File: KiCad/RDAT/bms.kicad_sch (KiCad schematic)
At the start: 29 parts, among them Q1 NMOS, Q2 NMOS, U3 BQ7791500PWT, U4 BQ34Z100PWR-R2

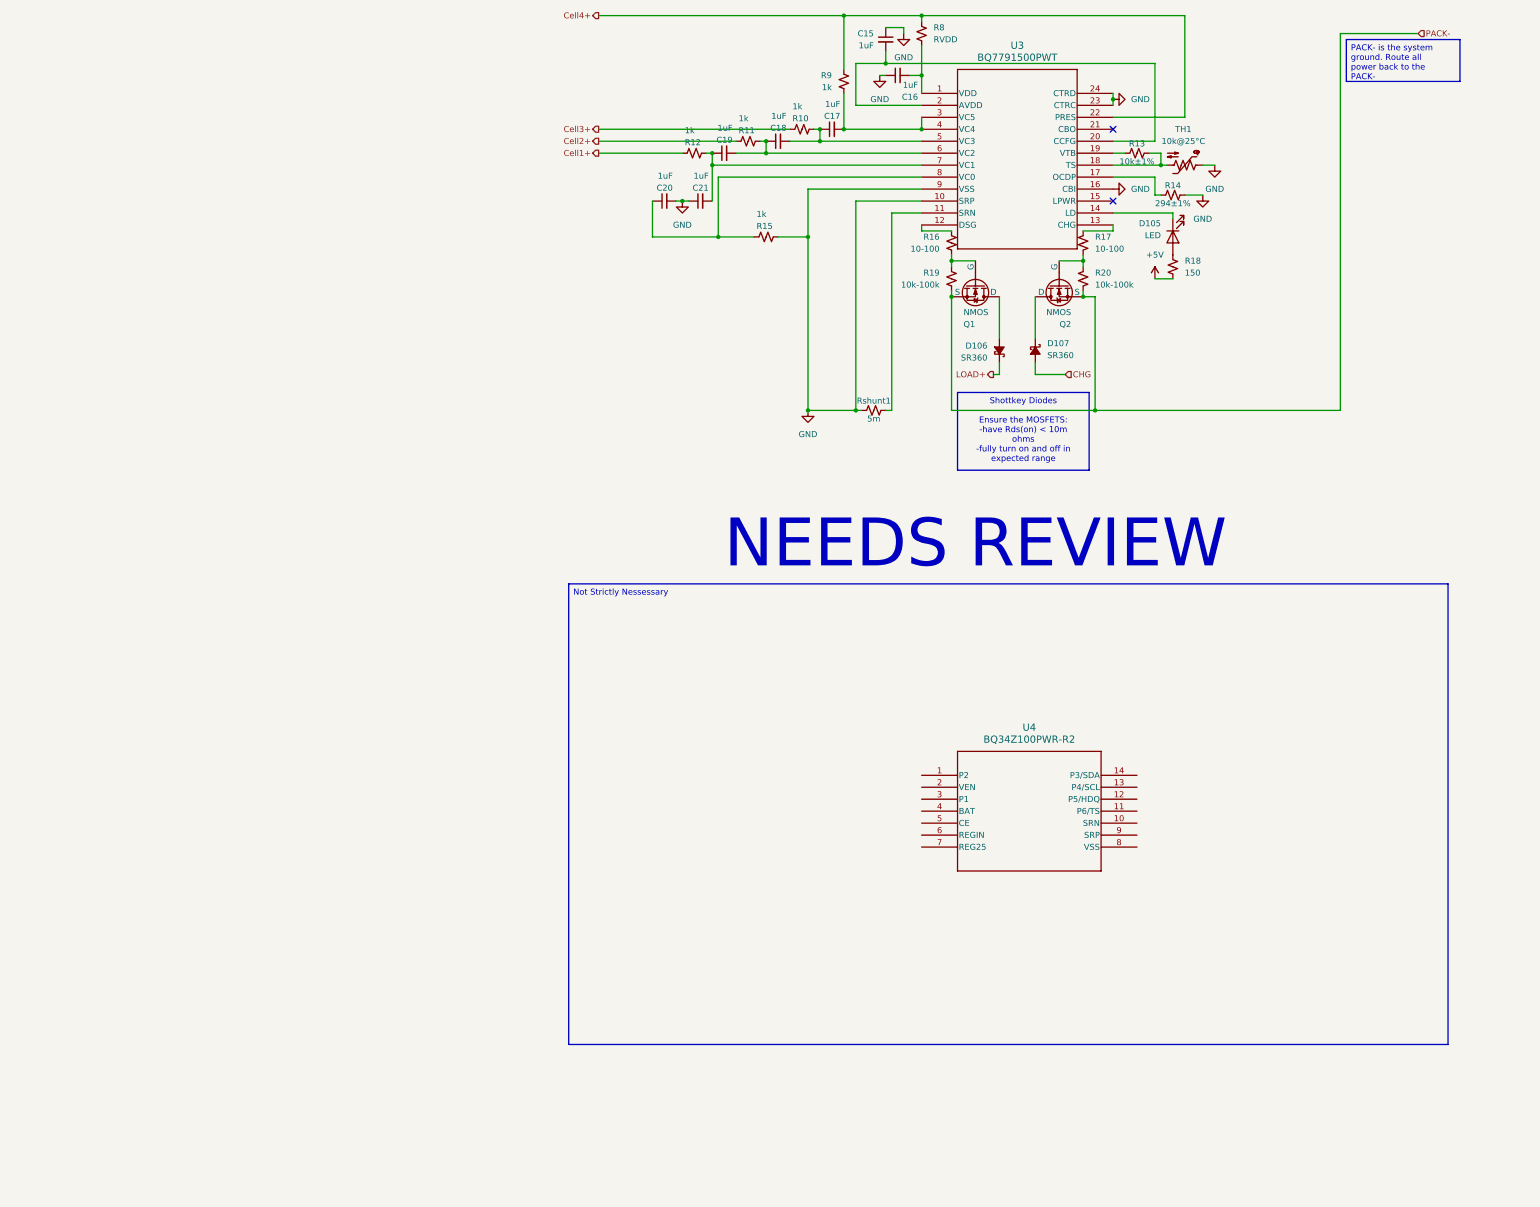
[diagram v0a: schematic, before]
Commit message: Started process of BMS review
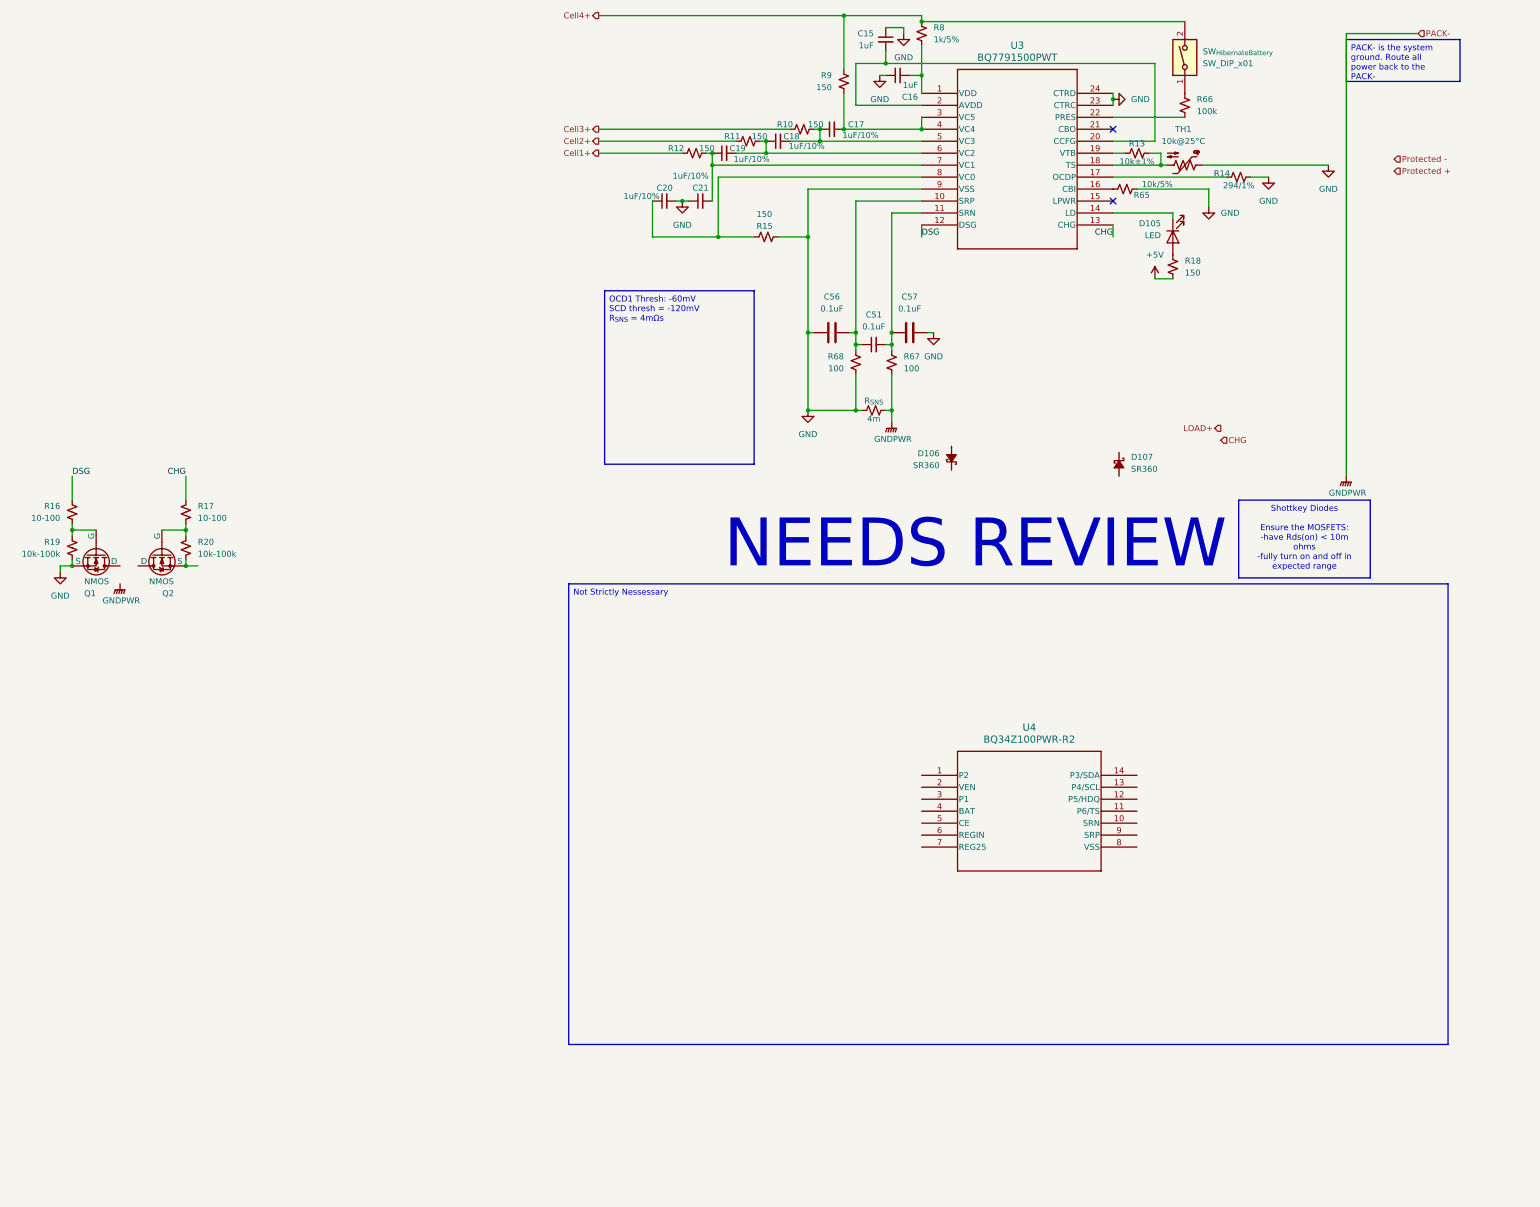
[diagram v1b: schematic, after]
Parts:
- added C51: 0.1uF, symbol Device:C_Small
- added C56, C57: 0.1uF, symbol Device:C
- added R65: 10k/5%, symbol Device:R_Small_US
- added R66: 100k, symbol Device:R_Small_US
- added R67, R68: 100, symbol Device:R_Small_US
- added SW_{HibernateBattery}: SW_DIP_x01, symbol Switch:SW_DIP_x01
- C17, C18, C19, C20, C21: value 1uF -> 1uF/10%
- R10, R11, R12, R15, R9: value 1k -> 150
- R14: value 294±1% -> 294/1%
- R8: value RVDD -> 1k/5%
- R_{SNS}: renamed from Rshunt1; value 5m -> 4m
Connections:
- net CHG: now also R17.1, U3.13 (CHG); no longer D107.2 (A)
- net Cell4+: now also SW_{HibernateBattery}.2; no longer U3.22 (PRES)
- net GND: now also Q1.3 (S), R19.2, C56.1, C57.2, R65.2, R68.2; no longer U3.10 (SRP), U3.16 (CBI)
- net LOAD+: no longer D106.1 (K)
- net at Q2.1 (D): no longer D107.1 (K)
- net at U3.11 (SRN): now also C51.2, C57.1, R67.1; no longer R_{SNS}.2
- net DSG: now reaches R16.1, U3.12 (DSG)
- net at Q1.1 (D): no longer D106.2 (A)
- net PACK-: no longer names the net of Q2.3 (S), R20.2
- net PACK-: no longer Q1.3 (S), R19.2
- new net: C51.1, C56.2, R68.1, U3.10 (SRP)
- new net: R66.1, SW_{HibernateBattery}.1
- new net: R66.2, U3.22 (PRES)
- new net: R65.1, U3.16 (CBI)
- new net GNDPWR: R67.2, R_{SNS}.2
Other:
- moved on the sheet: D106, D107, Q1, Q2, R14, R16, R17, R19, R20

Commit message: 2x checked all schematics
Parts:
- removed C18, C19, C20, C21: 1uF/10%, symbol Device:C_Small
- removed C51: 0.1uF, symbol Device:C_Small
- removed C56, C57: 0.1uF, symbol Device:C
- removed D105: LED, symbol Device:LED
- removed D106, D107: SR360, symbol Device:D_Schottky_Small_Filled
- removed R11, R12, R15, R18: 150, symbol Device:R_Small_US
- removed R14: 294/1%, symbol Device:R_Small_US
- removed R65: 10k/5%, symbol Device:R_Small_US
- removed R67, R68: 100, symbol Device:R_Small_US
- removed R_{SNS}: 4m, symbol Device:R_Small_US
- added C58, C59, C62, C63: 1uF/10%, symbol Device:C_Small
- added C64, C67: 0.1uF, symbol Device:C
- added C65: 0.1uF, symbol Device:C_Small
- added R101, R103, R94: 150, symbol Device:R_Small_US
- added R102, R104: 100, symbol Device:R_Small_US
- added R16: R_Small_US, symbol Device:R_Small_US
- added R17: 470, symbol Device:R_Small_US
- added R85: 1k/5%, symbol Device:R_Small_US
- added R_{SNS}1: 4m, symbol Device:R_Small_US
- R8: value 1k/5% -> 450k
- R_{CHG}1: renamed from R17; value 10-100 -> 220/5%
- R_{DSG}1: renamed from R16; value 10-100 -> 470/5%
- R_{GS}1: renamed from R19; value 10k-100k -> 4.7M
- R_{GS}2: renamed from R20; value 10k-100k -> 4.7M
- U4: now not fitted
- renumbered SW_{HibernateBattery} to SW_{HibernateBattery}1, TH1 to TH_103AT_1
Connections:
- net Cell1+: now also R101.2
- net Cell2+: now also R94.2
- net Cell3+: now also R10.2; no longer R10.1
- net Cell4+: now also R85.1; no longer R8.1
- net SRP: now reaches U3.10 (SRP)
- net SRP: now also C65.2, C67.1, R102.2
- net SRN: now reaches U3.11 (SRN)
- net SRN: now also C64.2, C65.1, R104.2
- net at Q2.1 (D): now also Q1.1 (D)
- net SYS_BAT-: now reaches Q2.3 (S), R_{GS}2.2
- net SYS_BAT-: now also R8.2
- net TS: now reaches R13.1
- net TS: now also TH_103AT_1.1, U3.18 (TS); no longer U3.19 (VTB)
- net VC0: now reaches U3.8 (VC0)
- net VC0: now also C63.1, R103.1
- net VC2: now reaches U3.6 (VC2)
- net VC2: now also C58.1, C59.2, R94.1
- net VC1: now reaches U3.7 (VC1)
- net VC1: now also C59.1, C62.2, R101.1
- net VC3: now reaches C17.1, U3.5 (VC3)
- net VC3: now also R10.1, C58.2; no longer R10.2
- net VDD: now reaches C16.2, U3.1 (VDD)
- net VDD: now also R85.2; no longer R8.2
- net PRES: now reaches R66.2, U3.22 (PRES)
- net at U3.16 (CBI): now also R16.1
- net VC4: now reaches C17.2, R9.2, U3.3 (VC5), U3.4 (VC4)
- net OCDP: now reaches U3.17 (OCDP)
- net OCDP: now also R17.1
- net LD: now reaches U3.14 (LD)
- net LD: now also R8.1
- net AVDD: now reaches U3.2 (AVDD), U3.20 (CCFG)
- net AVDD: now also C15.1; no longer C15.2
- net GND renamed Earth
- net Earth: now also C15.2, TH_103AT_1.2, C62.1, C63.2, C64.1, C67.2, R102.1, R103.2, R16.2, R17.2, R_{SNS}1.1; no longer C15.1, Q1.3 (S), R_{GS}1.2, TH_103AT_1.1
- new net Q_DSG_S: Q1.3 (S), R104.1, R_{GS}1.2, R_{SNS}1.2
- new net VTB: R13.2, U3.19 (VTB)
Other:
- note removed: "NEEDS REVIEW"
- moved on the sheet: C15, C16, C17, Q1, Q2, R13, R66, R9, R_{CHG}1, R_{DSG}1, R_{GS}1, R_{GS}2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

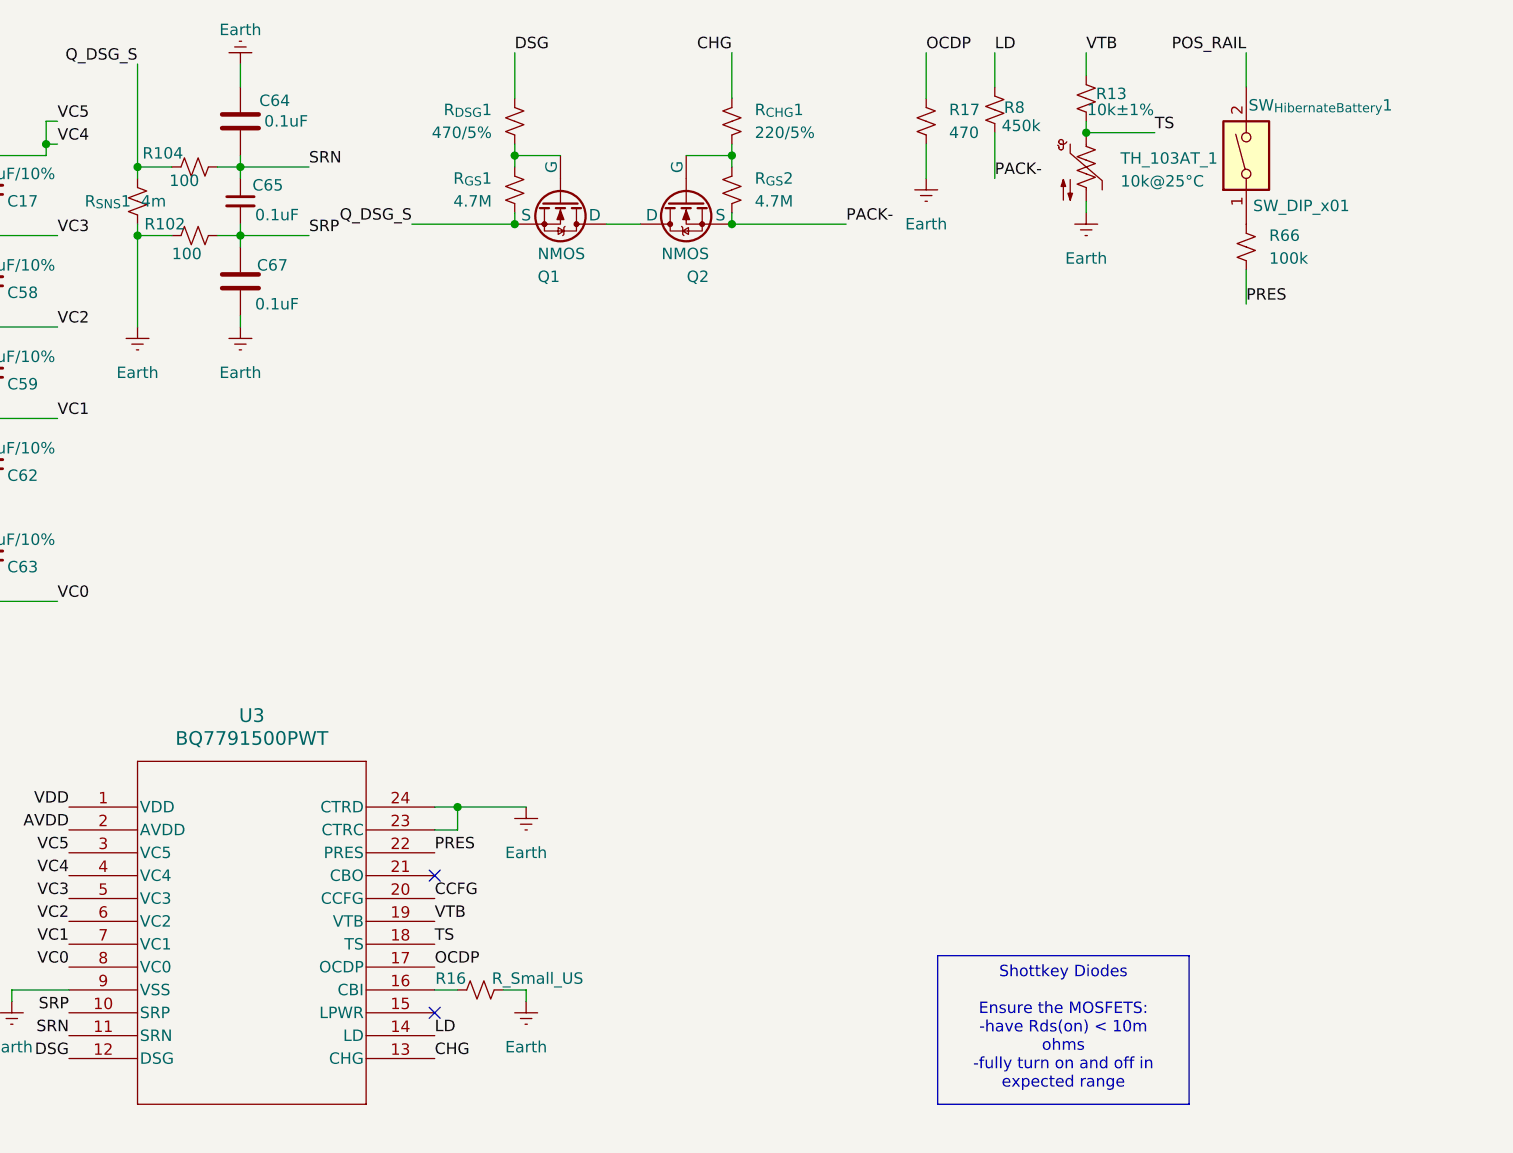
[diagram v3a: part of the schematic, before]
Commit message: Added Libs and DOCS
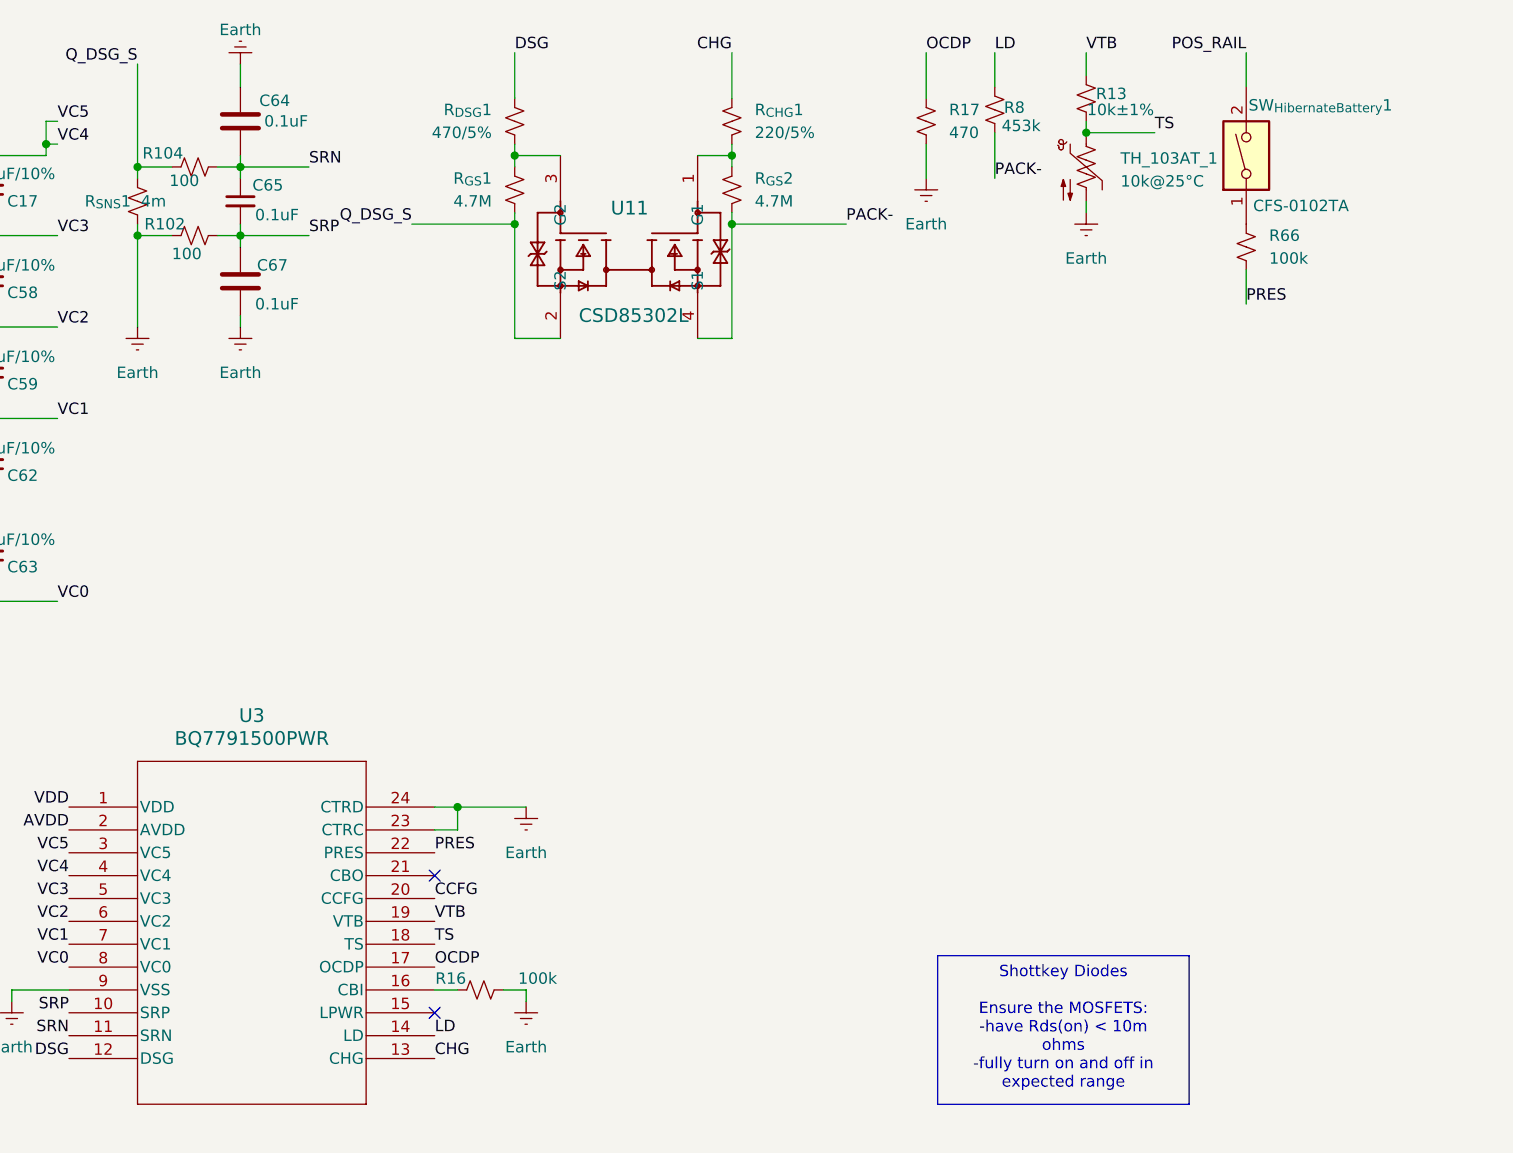
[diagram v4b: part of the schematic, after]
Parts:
- removed Q1, Q2: NMOS, symbol Simulation_SPICE:NMOS
- added U11: CSD85302L, YME0004A-MFG, symbol CSD85302L:CSD85302L
- C15, C16, C17, C58, C59, C62, C63: footprint (none) -> Capacitor_SMD:C_0402_1005Metric; JLCPCB_LINK (none) -> https://jlcpcb.com/partdetail/53938-CL05A105KA5NQNC/C52923
- C64, C65, C67: footprint (none) -> Capacitor_SMD:C_0402_1005Metric; JLCPCB_LINK (none) -> https://jlcpcb.com/partdetail/1933-0402F104M500NT/C1581
- R10, R101, R103, R9, R94: footprint (none) -> Resistor_SMD:R_0402_1005Metric; JLCPCB_LINK (none) -> https://jlcpcb.com/partdetail/25825-0402WGF1500TCE/C25082
- R102, R104: footprint (none) -> Resistor_SMD:R_0402_1005Metric; JLCPCB_LINK (none) -> https://jlcpcb.com/partdetail/25819-0402WGF1000TCE/C25076
- R13: footprint (none) -> Resistor_SMD:R_0402_1005Metric; JLCPCB_LINK (none) -> https://jlcpcb.com/partdetail/26487-0402WGF1002TCE/C25744
- R16: value R_Small_US -> 100k; footprint (none) -> Resistor_SMD:R_0402_1005Metric; JLCPCB_LINK (none) -> https://jlcpcb.com/partdetail/26484-0402WGF1003TCE/C25741
- R17, R_{DSG}1: footprint (none) -> Resistor_SMD:R_0402_1005Metric; JLCPCB_LINK (none) -> https://jlcpcb.com/partdetail/25860-0402WGF4700TCE/C25117
- R66: footprint (none) -> Resistor_SMD:R_0402_1005Metric; JLCPCB_LINK (none) -> https://jlcpcb.com/partdetail/26484-0402WGF1003TCE/C25741
- R8: value 450k -> 453k; footprint (none) -> Resistor_SMD:R_0402_1005Metric; JLCPCB_LINK (none) -> https://jlcpcb.com/partdetail/27758-0402WGF4533TCE/C27009
- R85: footprint (none) -> Resistor_SMD:R_0402_1005Metric; JLCPCB_LINK (none) -> https://jlcpcb.com/partdetail/12256-0402WGF1001TCE/C11702
- R_{CHG}1: footprint (none) -> Resistor_SMD:R_0402_1005Metric; JLCPCB_LINK (none) -> https://jlcpcb.com/partdetail/25834-0402WGF2200TCE/C25091
- R_{GS}1, R_{GS}2: footprint (none) -> Resistor_SMD:R_0402_1005Metric; JLCPCB_LINK (none) -> https://jlcpcb.com/partdetail/26834-0402WGJ0475TCE/C26091
- R_{SNS}1: footprint (none) -> Resistor_SMD:R_0402_1005Metric; JLCPCB_LINK (none) -> https://www.digikey.com/en/products/detail/vishay-dale/WFCP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
- SW_{HibernateBattery}1: value SW_DIP_x01 -> CFS-0102TA; footprint (none) -> footprints:SW_CFS-0102MA_NDC-L; JLCPCB_LINK (none) -> https://jlcpcb.com/partdetail/Nidec-CFS0102TA/C2921576
- TH_103AT_1: footprint (none) -> Resistor_SMD:R_0201_0603Metric; JLCPCB_LINK (none) -> https://jlcpcb.com/partdetail/MurataElectronics-NCP18XH103F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
- U3: value BQ7791500PWT -> BQ7791500PWR; JLCPCB_LINK (none) -> https://jlcpcb.com/partdetail/TexasInstruments-BQ7791500PWR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
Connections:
- net Q_DSG_S: now also U11.2 (S2)
- net SYS_BAT-: now also U11.4 (S1)
- net at R_{CHG}1.2, R_{GS}2.1: now also U11.1 (G1)
- net at R_{DSG}1.2, R_{GS}1.1: now also U11.3 (G2)

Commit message: Push before Board Layout
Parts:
- U11: footprint YME0004A-MFG -> footprints:YME0004A-MFG
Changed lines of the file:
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@@
 			)
 		)
-		(property "Footprint" "YME0004A-MFG"
+		(property "Footprint" "footprints:YME0004A-MFG"
 			(at 129.54 27.94 0)
 			(effects
